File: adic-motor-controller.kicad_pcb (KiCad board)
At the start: 2 copper layers, 28 parts, among them K1 CONN_3, K2 CONN_3, K3 CONN_3, K4 CONN_3, P1 CONN_6, U1 TLV5620C, U2 LM358, U3 LM358, U4 LM358, U5 LM358

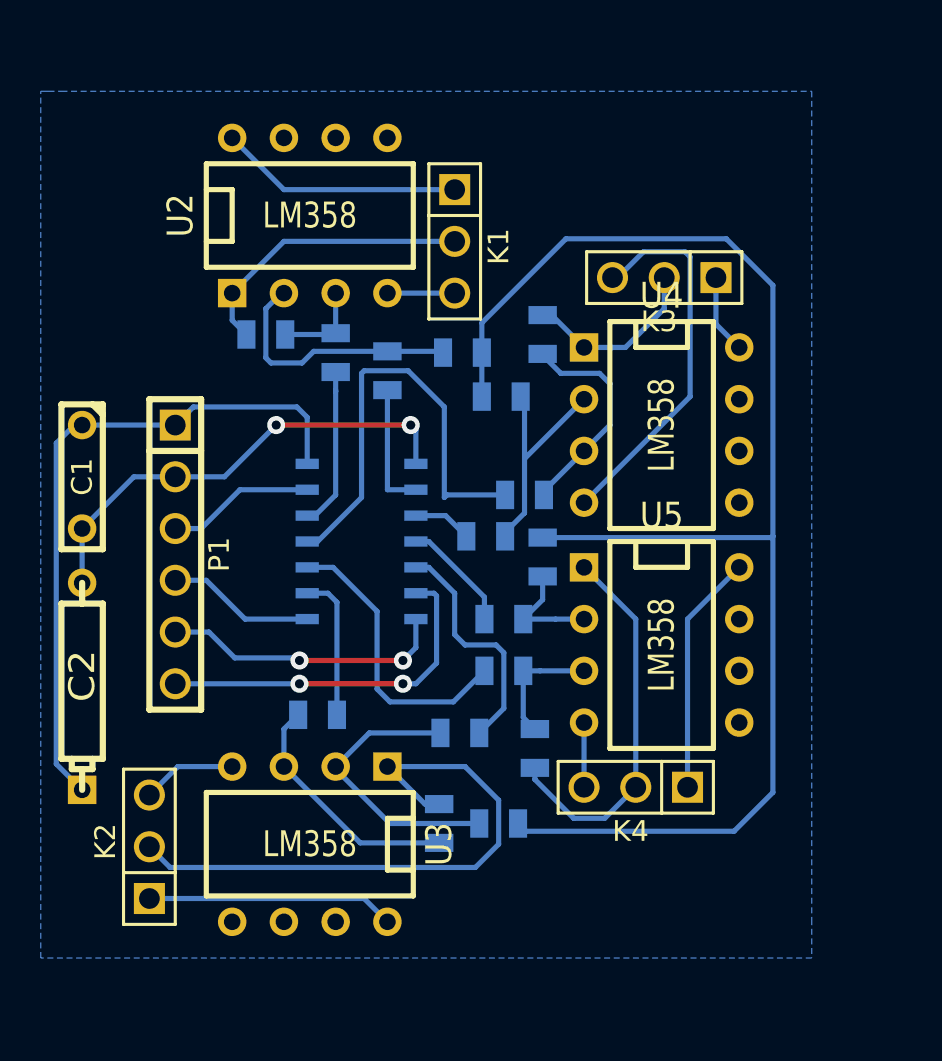
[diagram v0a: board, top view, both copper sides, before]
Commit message: Add GND net connection to op-ams
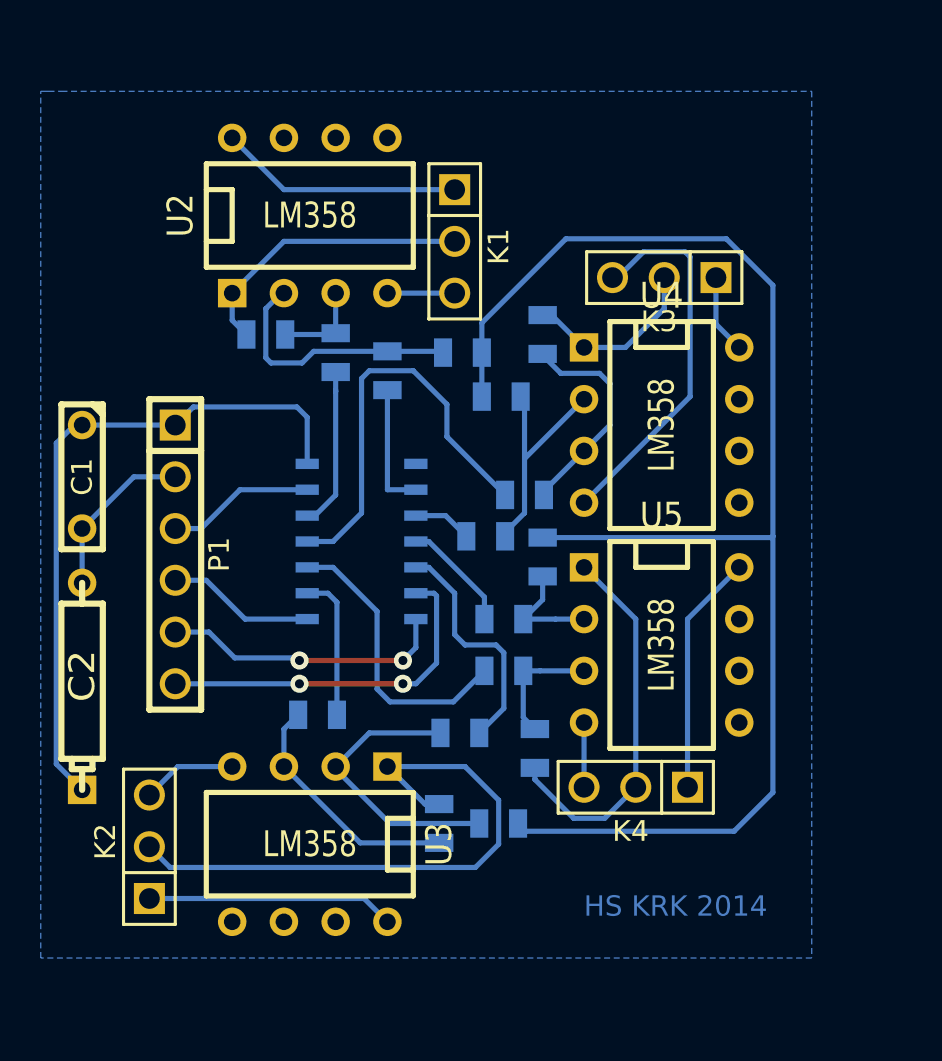
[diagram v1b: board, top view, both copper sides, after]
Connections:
- C1 pad 2: N-0000027 (its old number) -> GND
- C2 pad 2: N-0000027 (its old number) -> GND
- P1 pad 2: N-0000027 (its old number) -> GND
- U1 pad 1: N-0000027 (its old number) -> GND
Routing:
- net N-0000027 (its old number): track 22.9 -> 0.00 mm, vias 2 -> 0
- net GND: track 70.2 -> 78.5 mm
- net N-0000027: track 22.0 -> 20.5 mm
- added copper zone on B.Cu, net GND
- removed copper zone on B.Cu, net (none)
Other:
- board text added: "HS KRK 2014"

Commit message: Zwarcie nieużywanych wejść do masy.
Zmiana planowania. Rozszenie możliwośći.
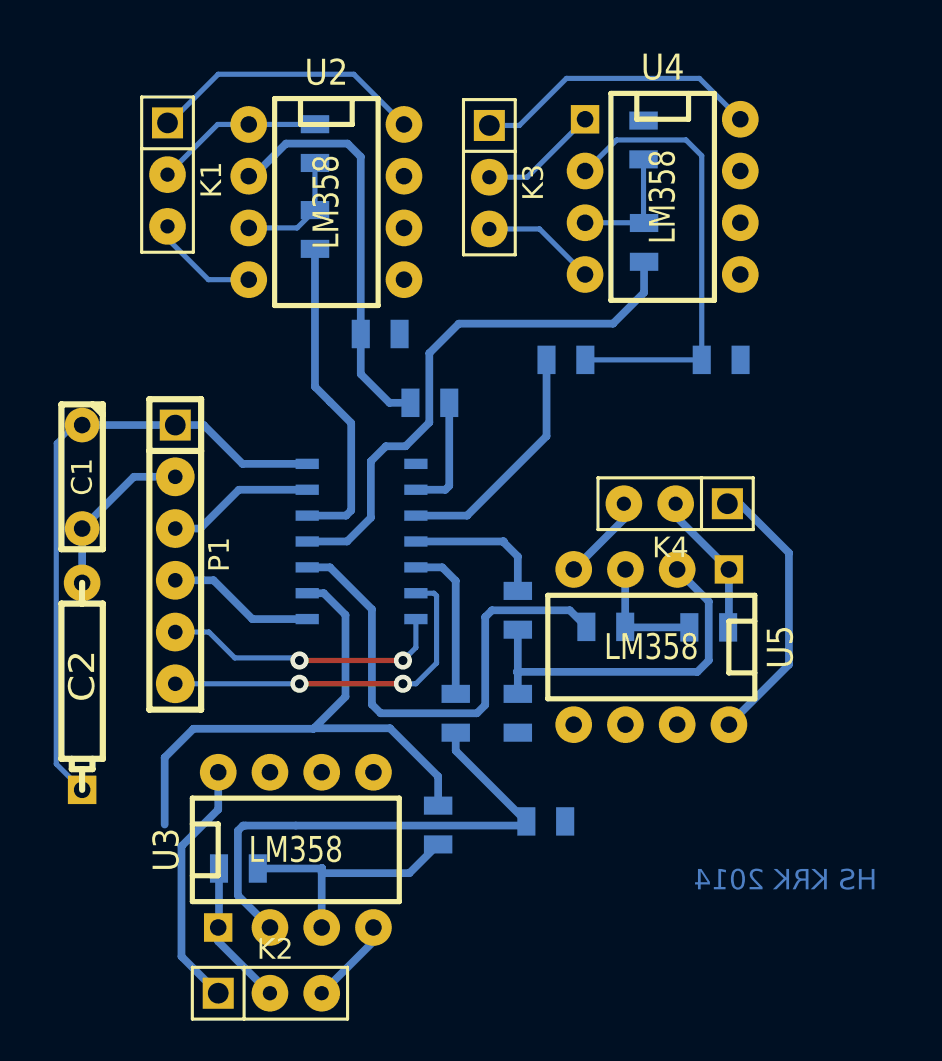
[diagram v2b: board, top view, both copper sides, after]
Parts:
- moved K1 14.5 mm to (49.9, 40.2)
- moved K4 14.1 mm to (74.9, 56.3)
- moved R9 13.7 mm to (73.3, 43.5), turned to 90 degrees
- moved U4 11.2 mm to (74.2, 41.2)
- moved R13 10.9 mm to (77.1, 49.3), turned to 180 degrees
- moved R15 10.8 mm to (73.3, 38.5)
- moved R16 10.4 mm to (76.5, 62.4), turned to 0 degrees
- moved R8 10.1 mm to (53.4, 74.2), turned to 180 degrees
- moved K3 9.90 mm to (65.7, 40.3), turned to 270 degrees
- moved R7 9.68 mm to (57.1, 38.6), turned to 90 degrees
- moved R10 9.51 mm to (69.5, 49.3)
- moved K2 9.31 mm to (54.9, 80.3), turned to 0 degrees
- moved R3 8.02 mm to (63.2, 72.1), turned to 270 degrees
- moved R14 7.77 mm to (67.1, 66.6), turned to 90 degrees
- moved R1 6.13 mm to (57.1, 42.8)
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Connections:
- U2 pad 5: (no net) -> GND
- U2 pad 6: (no net) -> GND
- U3 pad 5: (no net) -> GND
- U3 pad 6: (no net) -> GND
- U4 pad 5: (no net) -> GND
- U4 pad 6: (no net) -> GND
- U5 pad 5: (no net) -> GND
- U5 pad 6: (no net) -> GND
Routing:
- net GND: track 78.5 -> 8.29 mm
- net N-0000038: track 29.6 -> 7.19 mm
- net N-0000018: track 7.17 -> 28.2 mm
- net N-0000031: track 18.7 -> 5.62 mm
- net N-0000042: track 5.47 -> 18.0 mm
- net N-0000014: track 18.8 -> 7.17 mm
- net N-0000039: track 14.1 -> 25.5 mm
- net N-0000013: track 11.4 -> 22.4 mm
- net N-0000030: track 3.90 -> 14.1 mm
- net N-0000016: track 14.3 -> 24.4 mm
- net N-000004: track 2.90 -> 11.8 mm
- net N-0000010: track 7.91 -> 15.8 mm
- net N-0000044: track 12.7 -> 20.1 mm
- net N-000008: track 20.5 -> 26.7 mm
- net N-0000036: track 14.3 -> 8.26 mm
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- removed copper zone on B.Cu, net GND
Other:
- net class Default: trace_width 0.254 -> 0.38
